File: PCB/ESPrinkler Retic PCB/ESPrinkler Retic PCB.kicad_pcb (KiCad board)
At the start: 2 copper layers, 120.4 x 90.9 mm, 158 parts, among them J4 Conn_01x19, J5 Conn_01x19, J6 Conn_01x04, Q1 AO3400A, Q10 AO3400A, Q11 AO3400A, Q2 AO3400A, Q3 AO3400A, Q4 AO3400A, Q5 AO3400A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

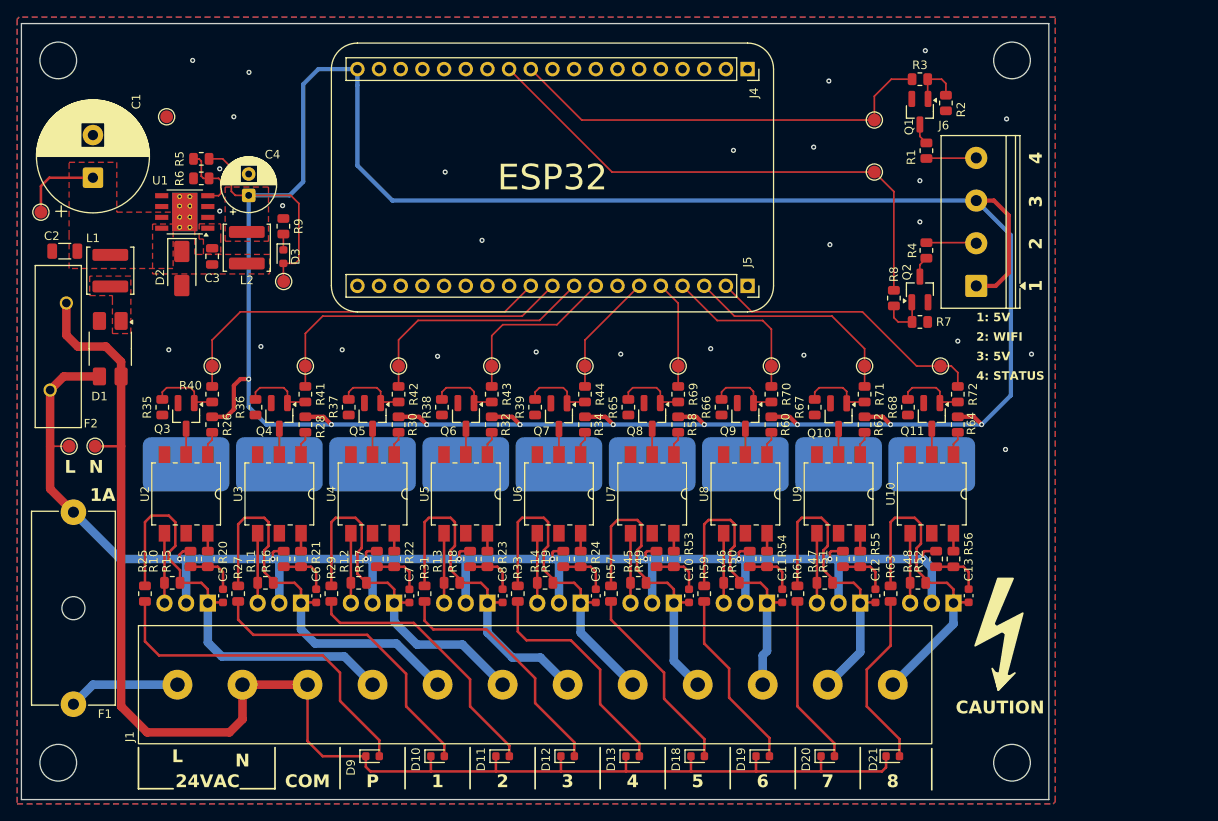
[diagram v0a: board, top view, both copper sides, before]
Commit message: Modify PCB layout & Export MFG files
Modified PCB layout after exporting mfg files and noticing some parts issues.
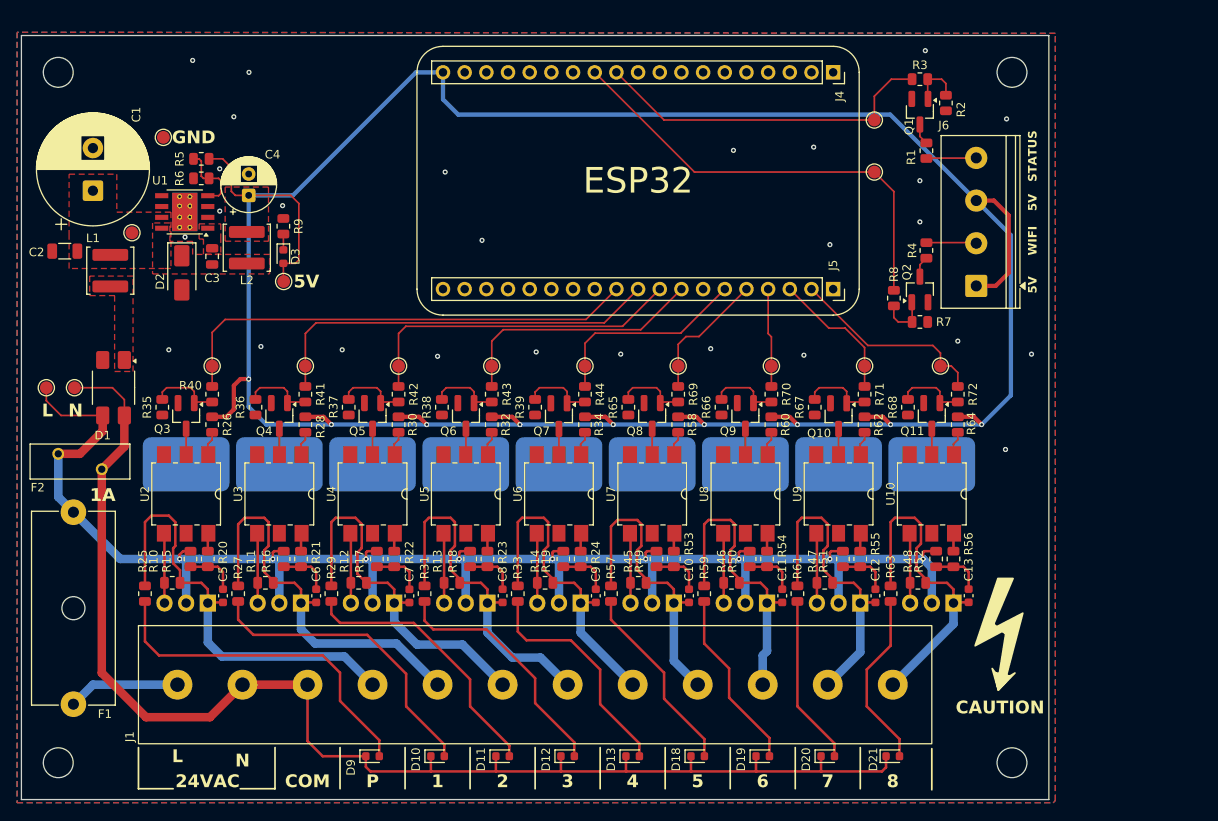
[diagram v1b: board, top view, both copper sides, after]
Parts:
- removed Hole_1, Hole_2, Hole_4 (x2): MountingHole_4.3mm_M4_ISO14580, MountingHole:MountingHole_4.3mm_M4_ISO14580
- added REF**: MountingHole_3.5mm, MountingHole:MountingHole_3.5mm, F.Cu at (248.4, 145.8)
- added REF**: MountingHole_3.5mm, MountingHole:MountingHole_3.5mm, F.Cu at (248.4, 64.9)
- added REF**: MountingHole_3.5mm, MountingHole:MountingHole_3.5mm, F.Cu at (136.7, 64.9)
- added REF**: MountingHole_3.5mm, MountingHole:MountingHole_3.5mm, F.Cu at (136.7, 145.8)
- F2: footprint Fuse:Fuse_BelFuse_0ZRE0100FF_L18.7mm_W5.1mm -> Fuse:Fuse_BelFuse_0ZRE0033FF_L11.4mm_W3.8mm
- moved TP4 10.9 mm to (145.3, 83.7)
- moved J4 10.0 mm to (227.5, 64.9)
- moved J5 10.0 mm to (227.5, 90.3)
- moved F2 7.53 mm to (136.7, 109.6), turned to 0 degrees
- moved TP1 7.36 mm to (135.3, 101.9)
- moved TP2 7.27 mm to (138.6, 101.9)
- moved D1 4.59 mm to (143.1, 101.9)
- moved TP3 2.44 mm to (149.0, 72.5)
- moved C1 1.52 mm to (140.7, 78.8)
- moved D2 0.51 mm to (151.1, 88.4)
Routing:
- net NEUT: track 173.3 -> 158.0 mm
- net +5V: track 328.4 -> 316.6 mm
- net /ESP32/Pump: track 45.4 -> 55.8 mm
- net /ESP32/Zone 2: track 28.6 -> 39.0 mm
- net /ESP32/Status LED: track 50.8 -> 40.6 mm
- net /ESP32/WIFI LED: track 62.6 -> 52.4 mm
- net /ESP32/Zone 7: track 26.3 -> 16.2 mm
- net /ESP32/Zone 1: track 37.5 -> 47.3 mm
- net /ESP32/Zone 4: track 14.4 -> 24.1 mm
- net VCC: track 9.55 -> 0.00 mm
- net /ESP32/Zone 3: track 20.6 -> 30.1 mm
- net /ESP32/Zone 8: track 33.0 -> 23.7 mm
- net /ESP32/Zone 6: track 19.2 -> 11.6 mm
- net /ESP32/Zone 5: track 12.6 -> 15.6 mm
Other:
- board size 120.4 x 90.9 mm -> 120.4 x 89.5 mm
- board text added: "5V"
- board text added: "GND"
- board text added: "STATUS"
- board text added: "WIFI"
- board text removed: "1: 5V"
- board text removed: "2: WIFI"
- board text removed: "3: 5V"
- board text removed: "4: STATUS"

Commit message: Change FB array resistors
Change FB resistor values for step down converter, changing output voltage to be much closer to 5V.
Footprint of resistors changed.
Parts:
- R5: value 10k -> 53.6k; footprint Resistor_SMD:R_0805_2012Metric -> Resistor_SMD:R_0603_1608Metric
- R6: value 3k -> 10.2k; footprint Resistor_SMD:R_0805_2012Metric -> Resistor_SMD:R_0603_1608Metric
- moved TP7 35.6 mm to (263.0, 94.5)
- moved TP5 33.5 mm to (260.7, 88.3)
- moved J6 20.7 mm to (262.9, 81.0)
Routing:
- net +5V: track 316.6 -> 216.7 mm
- net /ESP32/WIFI LED: track 52.4 -> 0.00 mm
- net /ESP32/Status LED: track 40.6 -> 0.00 mm
- net Net-(Q2-G): track 6.04 -> 0.00 mm
- net Net-(Q1-G): track 6.04 -> 0.00 mm
- net Net-(J6-Pin_2): track 5.87 -> 0.00 mm
- net Net-(J6-Pin_4): track 5.85 -> 0.00 mm
- net Net-(Q2-D): track 2.48 -> 0.00 mm
- net Net-(Q1-D): track 2.48 -> 0.00 mm
- net GND: vias 27 -> 25

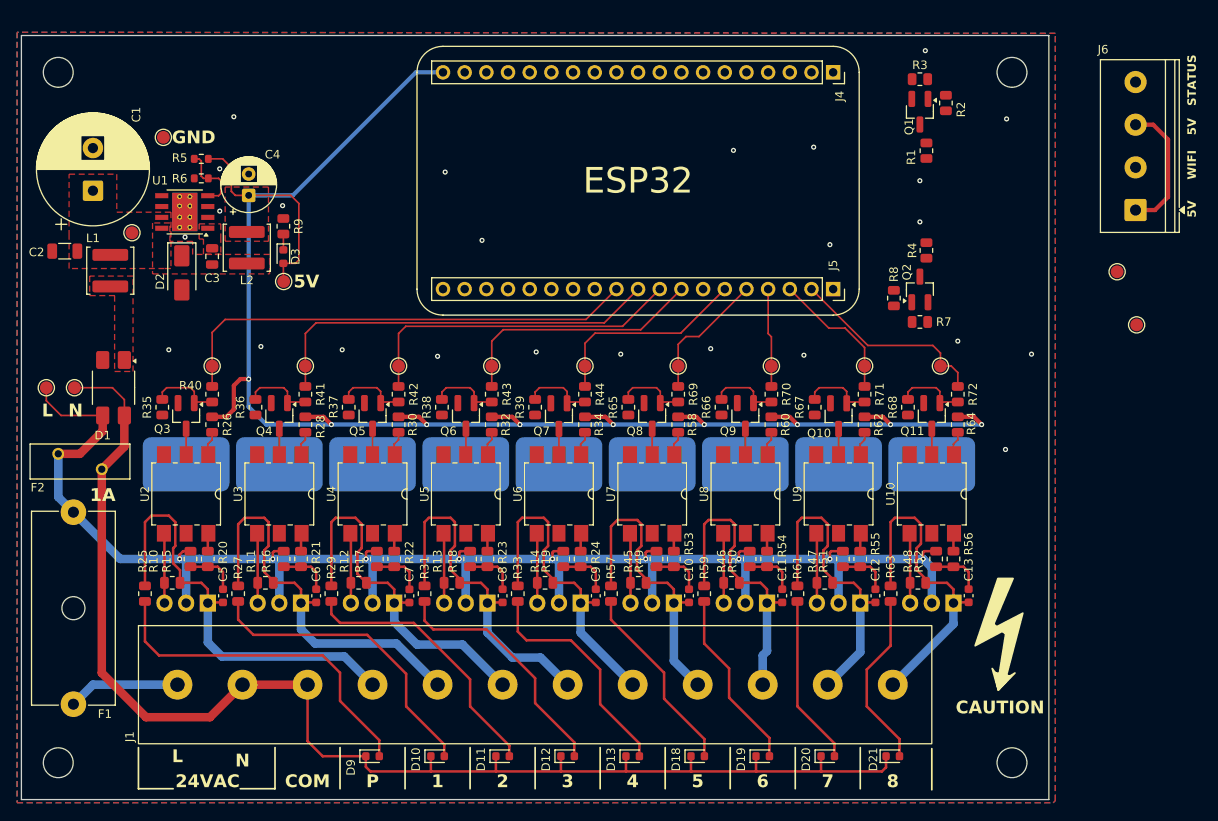
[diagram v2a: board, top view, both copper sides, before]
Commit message: Adjust PCB silkscreen text
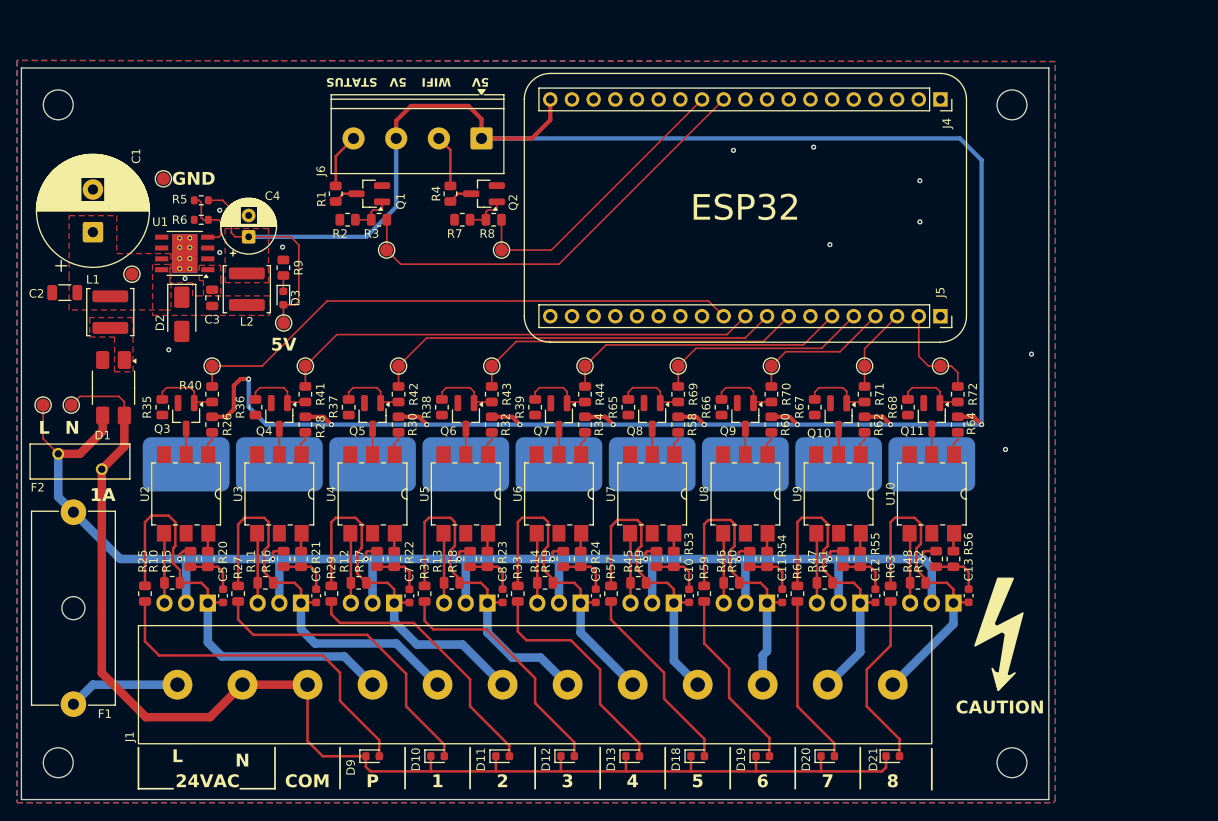
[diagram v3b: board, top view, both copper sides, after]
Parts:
- moved TP5 85.6 mm to (175.1, 85.7)
- moved J6 77.1 mm to (186.3, 72.6), turned to 180 degrees
- moved TP7 74.9 mm to (188.6, 85.7)
- moved R2 71.4 mm to (170.6, 82.2), turned to 0 degrees
- moved R1 69.4 mm to (169.2, 79.1), turned to 90 degrees
- moved R3 65.5 mm to (174.2, 82.2), turned to 180 degrees
- moved Q1 65.2 mm to (173.1, 79.1), turned to 180 degrees
- moved R4 56.2 mm to (182.6, 79.1)
- moved R7 54.9 mm to (184.0, 82.2), turned to 0 degrees
- moved Q2 52.3 mm to (186.5, 79.1), turned to 180 degrees
- moved R8 47.8 mm to (187.7, 82.2), turned to 180 degrees
- moved J5 13.0 mm to (240.0, 93.5)
- moved J4 13.0 mm to (240.0, 68.1)
- moved C1 4.86 mm to (140.7, 83.6)
- moved C4 4.86 mm to (159.0, 84.2)
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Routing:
- net +5V: track 216.7 -> 295.2 mm
- net /ESP32/Status LED: track 0.00 -> 51.7 mm
- net /ESP32/WIFI LED: track 0.00 -> 34.4 mm
- net /ESP32/Zone 8: track 23.7 -> 11.7 mm
- net /ESP32/Pump: track 55.8 -> 66.2 mm
- net /ESP32/Zone 5: track 15.6 -> 25.4 mm
- net /ESP32/Zone 4: track 24.1 -> 33.8 mm
- net /ESP32/Zone 3: track 30.1 -> 39.6 mm
- net /ESP32/Zone 2: track 39.0 -> 48.0 mm
- net /ESP32/Zone 1: track 47.3 -> 56.4 mm
- net Net-(J6-Pin_4): track 0.00 -> 6.43 mm
- net /ESP32/Zone 7: track 16.2 -> 9.81 mm
- net Net-(J6-Pin_2): track 0.00 -> 6.13 mm
- net /ESP32/Zone 6: track 11.6 -> 17.0 mm
- net Net-(Q2-G): track 0.00 -> 4.96 mm
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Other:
- board size 120.4 x 89.5 mm -> 120.4 x 85.7 mm

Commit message: Prepare for V1.0 production
Export fab files for PCB manufacturing and parts ordering
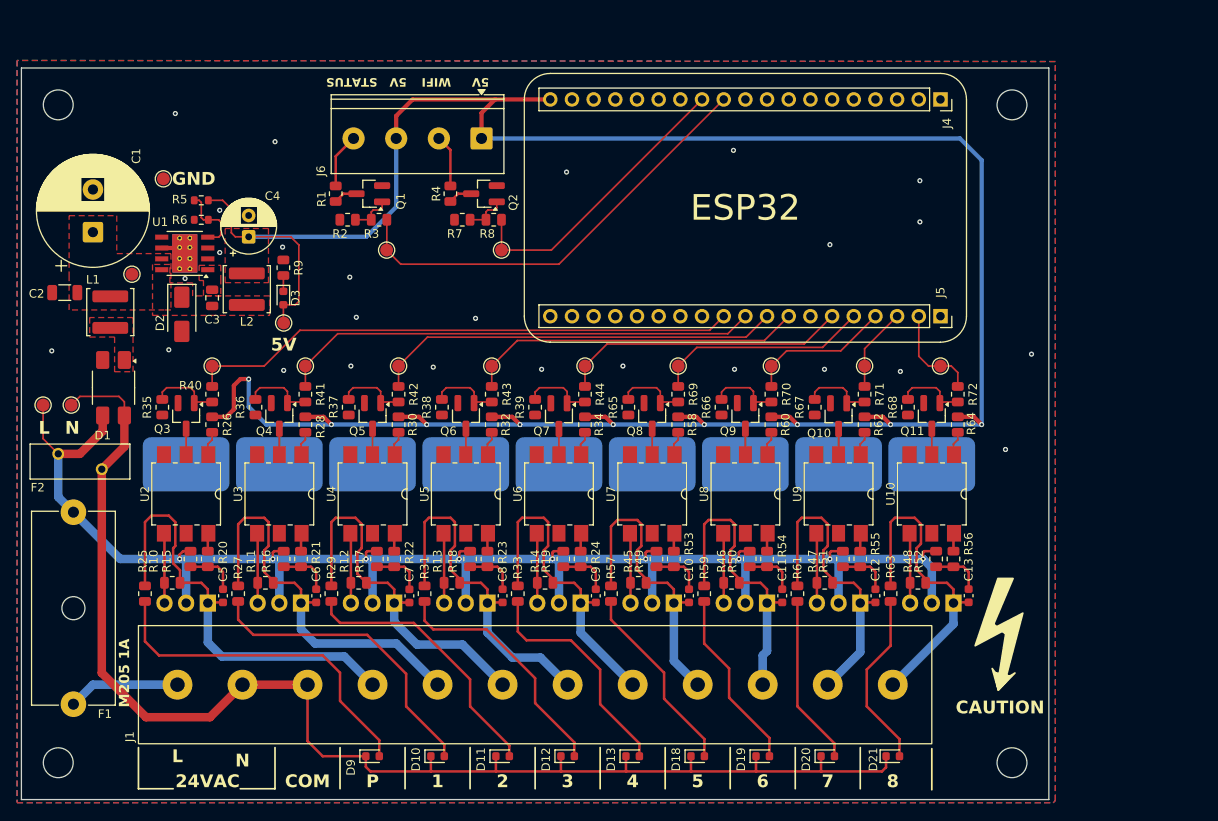
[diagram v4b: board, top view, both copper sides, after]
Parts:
- C10, C11, C12, C13, C5, C6, C7, C8, C9: value 12pF -> 2.2nF
- R15, R16, R17, R18, R19, R49, R50, R51, R52: value 1.2k -> 300R
- R20, R21, R22, R23, R24, R53, R54, R55, R56: value 68R -> 22R
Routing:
- net GND: track 0.00 -> 3.81 mm, vias 12 -> 26
- net /ESP32/Pump: track 66.2 -> 64.8 mm
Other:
- board text added: "M205 1A"
- board text removed: "1A"

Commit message: PCB version 1.1 following peer review
PTC in line with live, previously shorted between live and neutral.
Added boxes around sections on schematic for better readability.
Modified terminal block silkscreen to make more sense
Modified routing of 5V power to to reduce tunnels and traces on bottom plane.
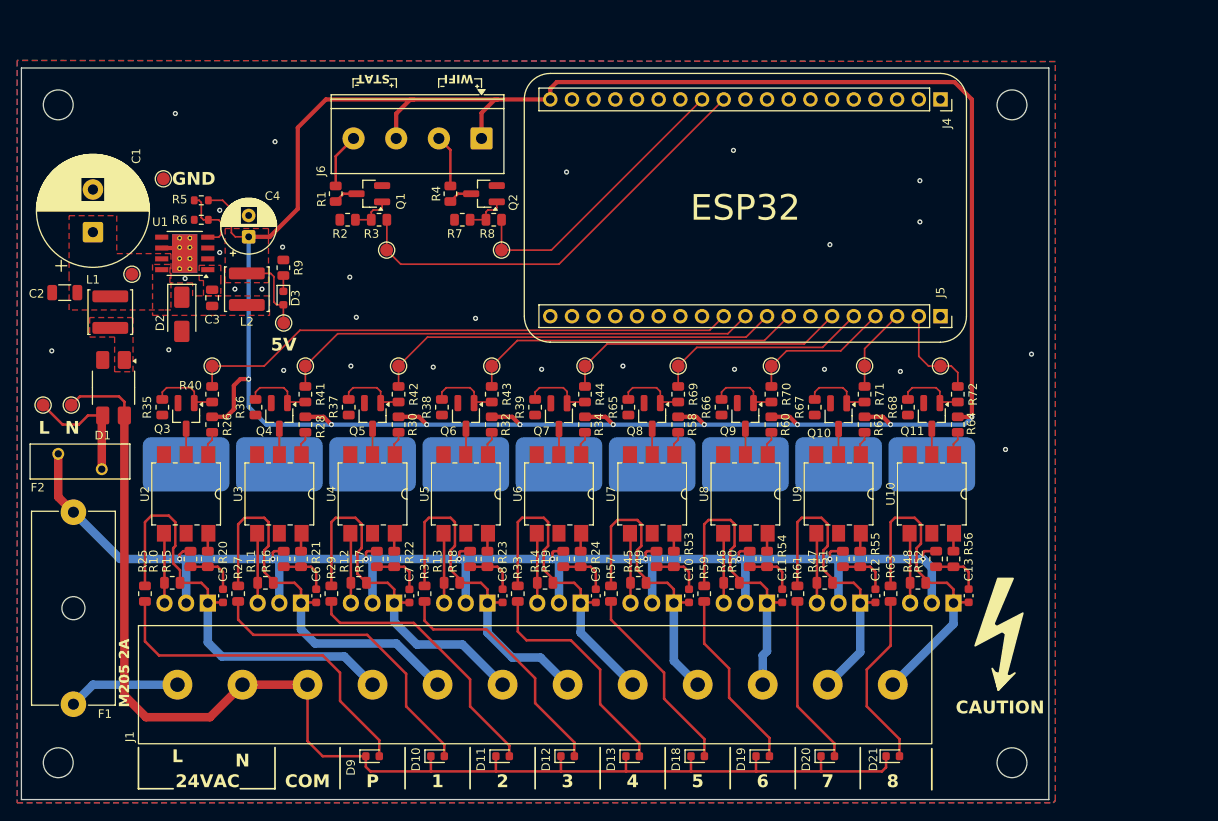
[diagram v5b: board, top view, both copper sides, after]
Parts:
- F1: value 1A -> M205 2A
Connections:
- D14 pad 2: LIVE -> LIVE_SOLENOID
- D15 pad 2: LIVE -> LIVE_SOLENOID
- D16 pad 2: LIVE -> LIVE_SOLENOID
- D17 pad 2: LIVE -> LIVE_SOLENOID
- D4 pad 2: LIVE -> LIVE_SOLENOID
- D5 pad 2: LIVE -> LIVE_SOLENOID
- D6 pad 2: LIVE -> LIVE_SOLENOID
- D7 pad 2: LIVE -> LIVE_SOLENOID
- D8 pad 2: LIVE -> LIVE_SOLENOID
- F1 pad 2: LIVE -> LIVE_SOLENOID
- F2 pad 1: LIVE -> LIVE_SOLENOID
- F2 pad 2: NEUT -> LIVE
- R15 pad 1: LIVE -> LIVE_SOLENOID
- R16 pad 1: LIVE -> LIVE_SOLENOID
- R17 pad 1: LIVE -> LIVE_SOLENOID
- R18 pad 1: LIVE -> LIVE_SOLENOID
- R19 pad 1: LIVE -> LIVE_SOLENOID
- R49 pad 1: LIVE -> LIVE_SOLENOID
- R50 pad 1: LIVE -> LIVE_SOLENOID
- R51 pad 1: LIVE -> LIVE_SOLENOID
- R52 pad 1: LIVE -> LIVE_SOLENOID
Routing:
- net LIVE_SOLENOID: track 0.00 -> 175.5 mm, vias 0 -> 9
- net LIVE: track 190.1 -> 14.7 mm, vias 9 -> 0
- net +5V: track 294.9 -> 305.6 mm
- net NEUT: track 158.2 -> 156.0 mm
- net GND: vias 26 -> 28
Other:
- board text added: "M205 2A"
- board text added: "STAT"
- board text added: "VERSION: 1.1"
- board text removed: "M205 1A"
- board text removed: "STATUS"
- board text removed: "VERSION: 1.0"

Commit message: Continue V1.1 modifications
Round off corners on PCB
Remove solder mount for triacs, unnecessary addition. Can use adhesive if required to secure triacs.
Remove unnecessary vias between top and bottom ground planes
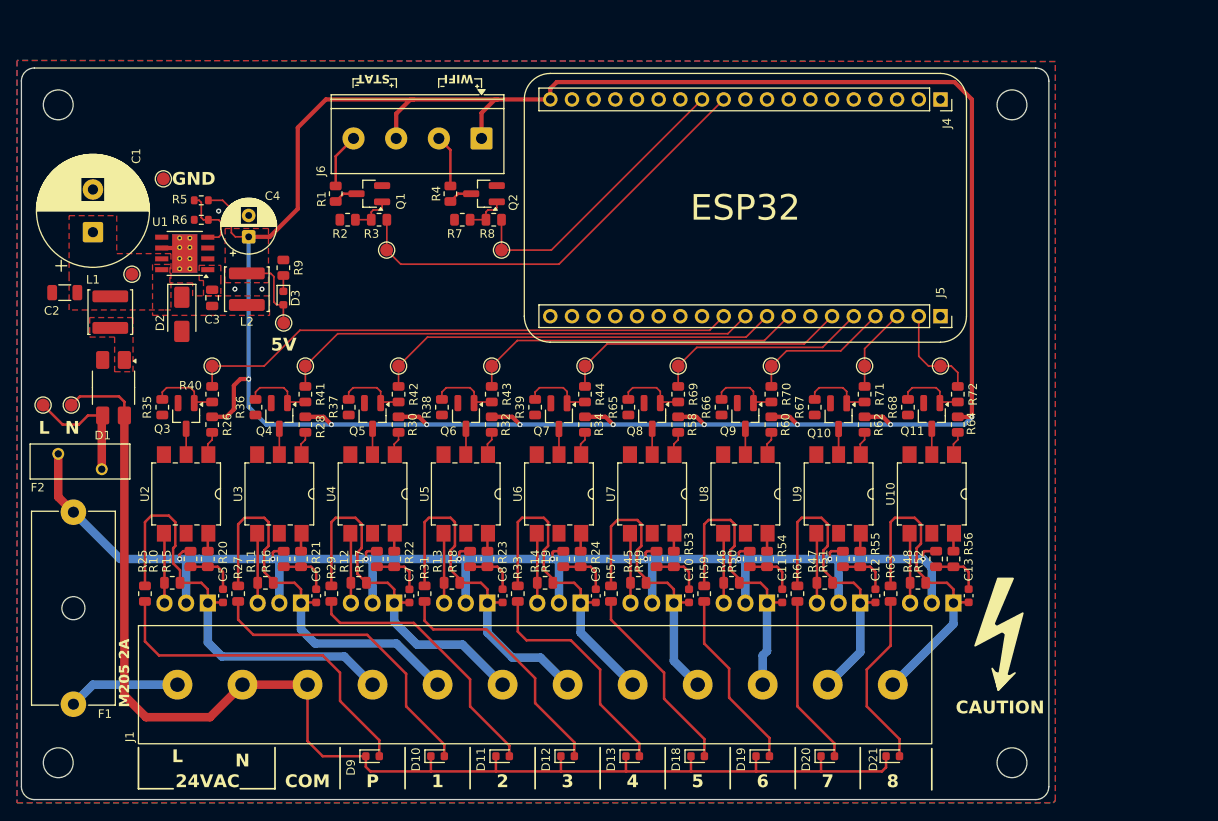
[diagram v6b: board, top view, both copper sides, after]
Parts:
- D14, D15, D16, D17, D4, D5, D6, D7, D8: footprint Footprints:TO-220-3_Horizontal_TabDown_Solder -> Footprints:TO-220-3_Horizontal_TabDown_NoHole
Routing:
- net GND: vias 28 -> 3
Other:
- outline, holes or cut-outs redrawn
